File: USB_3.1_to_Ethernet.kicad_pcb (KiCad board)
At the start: 4 copper layers, 75 x 25 mm, 93 parts, among them J1 RJ45_JK0654219, J2 USB3_A, U1 LAN7801_9JX, U2 93LC56B_SN, U3 KSZ9031RNXCC, U4 TLV76733, U5 USBLC6-2P6, U6 TPS7A0212, Y1 25MHz, Y2 25MHz

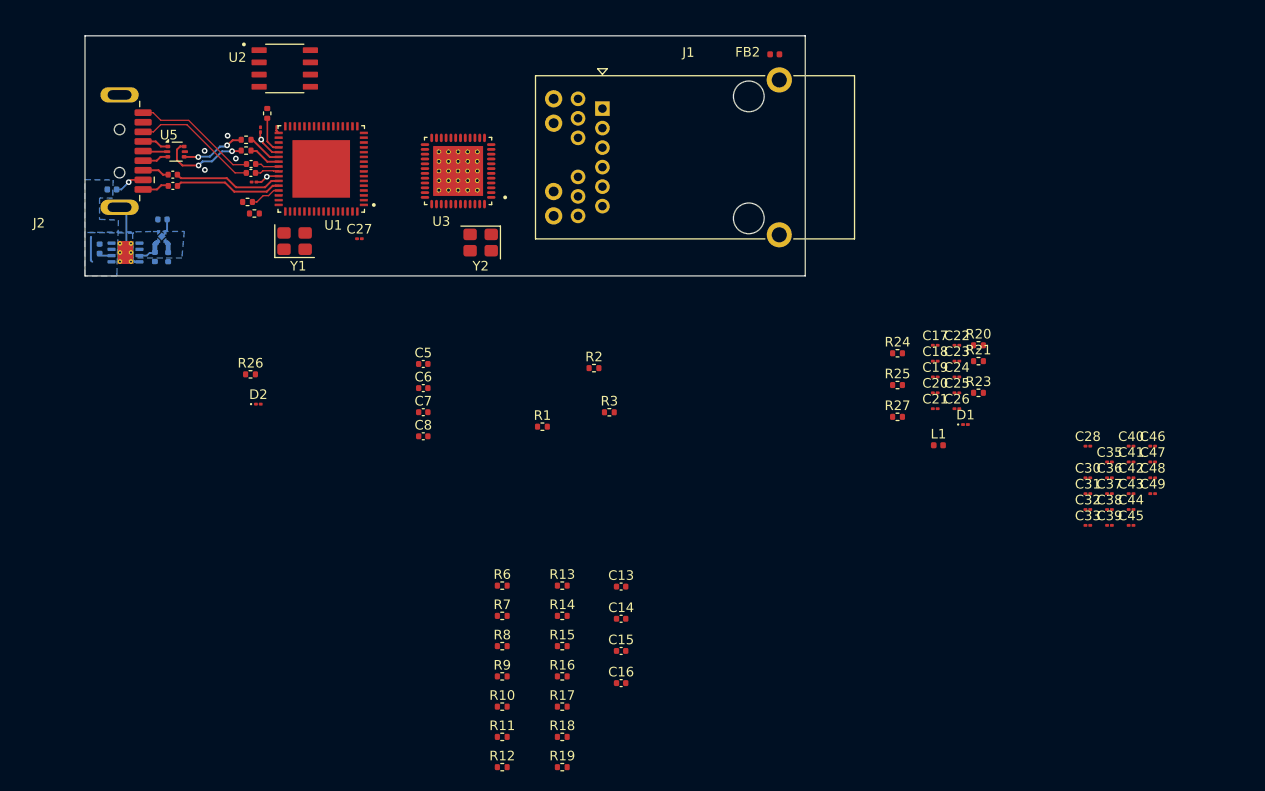
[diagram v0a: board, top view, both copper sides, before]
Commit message: 1. usb routing done 2.clock routing done 3. decoupling capacitors(3.3v) routing for lan7801 ic done
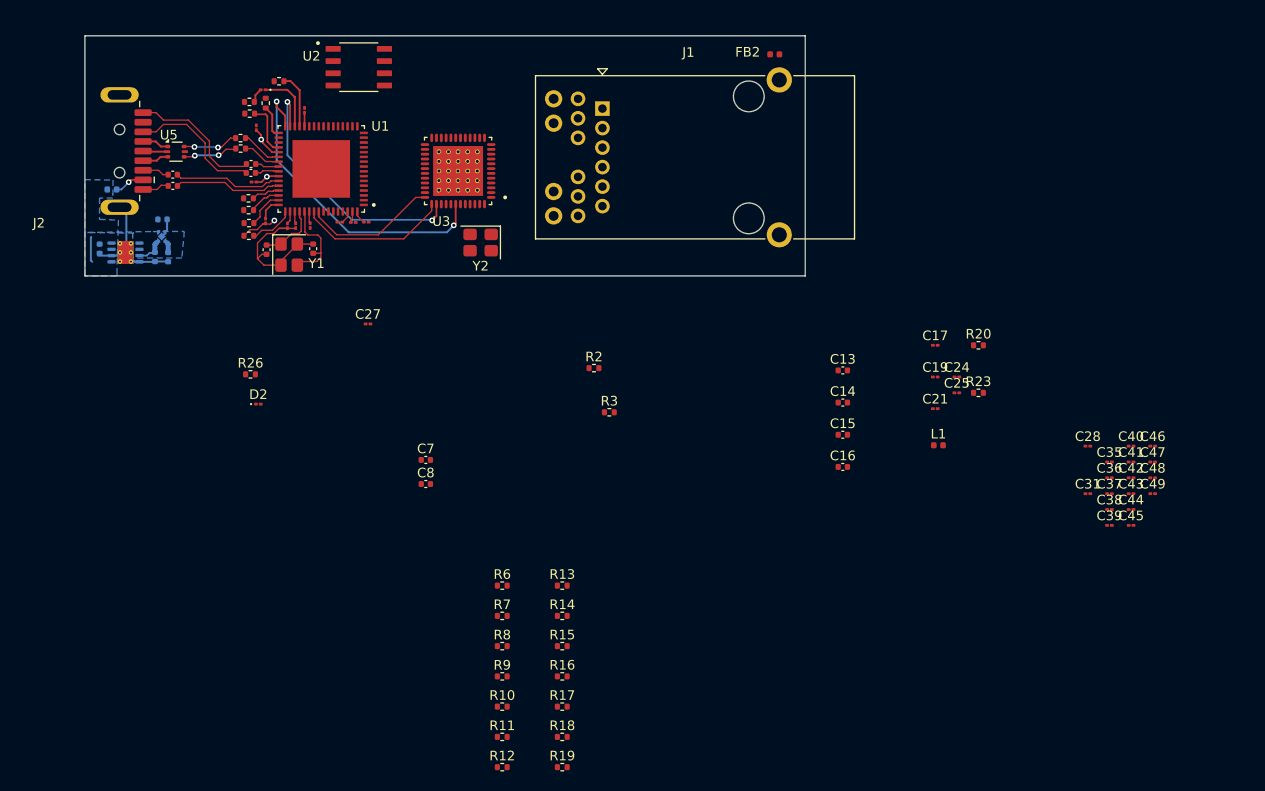
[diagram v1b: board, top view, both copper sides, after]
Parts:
- moved C30 90.1 mm to (82.6, 57.9), turned to 90 degrees
- moved C33 86.8 mm to (83.2, 69.9), turned to -90 degrees
- moved C32 83.4 mm to (86.2, 69.5), turned to 180 degrees
- moved D1 81.0 mm to (78.2, 55.7), turned to 180 degrees
- moved R21 78.9 mm to (78.5, 57.1), turned to -90 degrees
- moved R25 73.6 mm to (76.8, 57.0), turned to 180 degrees
- moved C18 71.2 mm to (78.5, 69.4), turned to -90 degrees
- moved C22 70.8 mm to (80.8, 69.9), turned to -90 degrees
- moved R27 70.5 mm to (76.8, 69.6), turned to 180 degrees
- moved R24 70.3 mm to (79.9, 54.8)
- moved C23 70.3 mm to (81.6, 69.9), turned to -90 degrees
- moved C26 65.8 mm to (87.6, 69.5)
- moved C20 61.9 mm to (89.0, 69.5)
- moved R1 36.5 mm to (76.8, 70.9), turned to 180 degrees
- moved C13 32.2 mm to (138.6, 84.9)
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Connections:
- C40 pad 1: Net-(C40-Pad1) -> 1v2_core
- C41 pad 1: Net-(C40-Pad1) -> 1v2_core
- C42 pad 1: Net-(C40-Pad1) -> 1v2_core
- C43 pad 1: Net-(C40-Pad1) -> 1v2_core
- C44 pad 1: Net-(C40-Pad1) -> 1v2_core
- C45 pad 1: Net-(C40-Pad1) -> 1v2_core
- C46 pad 1: Net-(C40-Pad1) -> 1v2_core
- C47 pad 1: Net-(C40-Pad1) -> 1v2_core
- C48 pad 1: Net-(C40-Pad1) -> 1v2_core
- C49 pad 1: Net-(C40-Pad1) -> 1v2_core
- R4 pad 2: D- -> D+
- R5 pad 2: D+ -> D-
- R6 pad 2: /TXD3 -> /TXD3_phy
- R7 pad 2: /TXD2 -> /TXD2_phy
- R8 pad 2: /TXD1 -> /TXD1_phy
- R9 pad 2: /TXD0 -> /TXD0_phy
- U3 pad 19: /TXD0 -> /TXD0_phy
- U3 pad 20: /TXD1 -> /TXD1_phy
- U3 pad 21: /TXD2 -> /TXD2_phy
- U3 pad 22: /TXD3 -> /TXD3_phy
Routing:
- net /~{RESET_N}: track 0.00 -> 33.2 mm, vias 0 -> 2
- net /INT_N/PME_N2: track 0.00 -> 28.0 mm, vias 0 -> 2
- net GND: track 12.8 -> 37.1 mm, vias 0 -> 1
- net /MDIO: track 0.00 -> 15.7 mm
- net /MDC: track 0.00 -> 14.0 mm
- net /XO_LAN: track 0.00 -> 9.68 mm
- net /~{SUSPEND_N}: track 0.00 -> 6.52 mm
- net 3v3_out: track 3.95 -> 10.3 mm
- net /XI_LAN: track 0.00 -> 6.31 mm
- net Net-(U1-VBUS_DET): track 0.00 -> 5.80 mm
- net Net-(U1-USBRBIAS): track 0.00 -> 4.69 mm
- net 1v2_core: track 5.81 -> 10.3 mm
- net Net-(U1-~{RESET_N}/PME_CLEAR): track 0.00 -> 3.96 mm
- net /Power section/_P: track 9.55 -> 5.81 mm
- net Net-(U1-TEST): track 0.00 -> 3.39 mm
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
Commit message: 1. RGMII routing done - LAN7801 RXD 2.Routing for RGMII - TXD on top layer done, bottom layer remaining 3. source termination resistors 27 ohm removed for RGMII
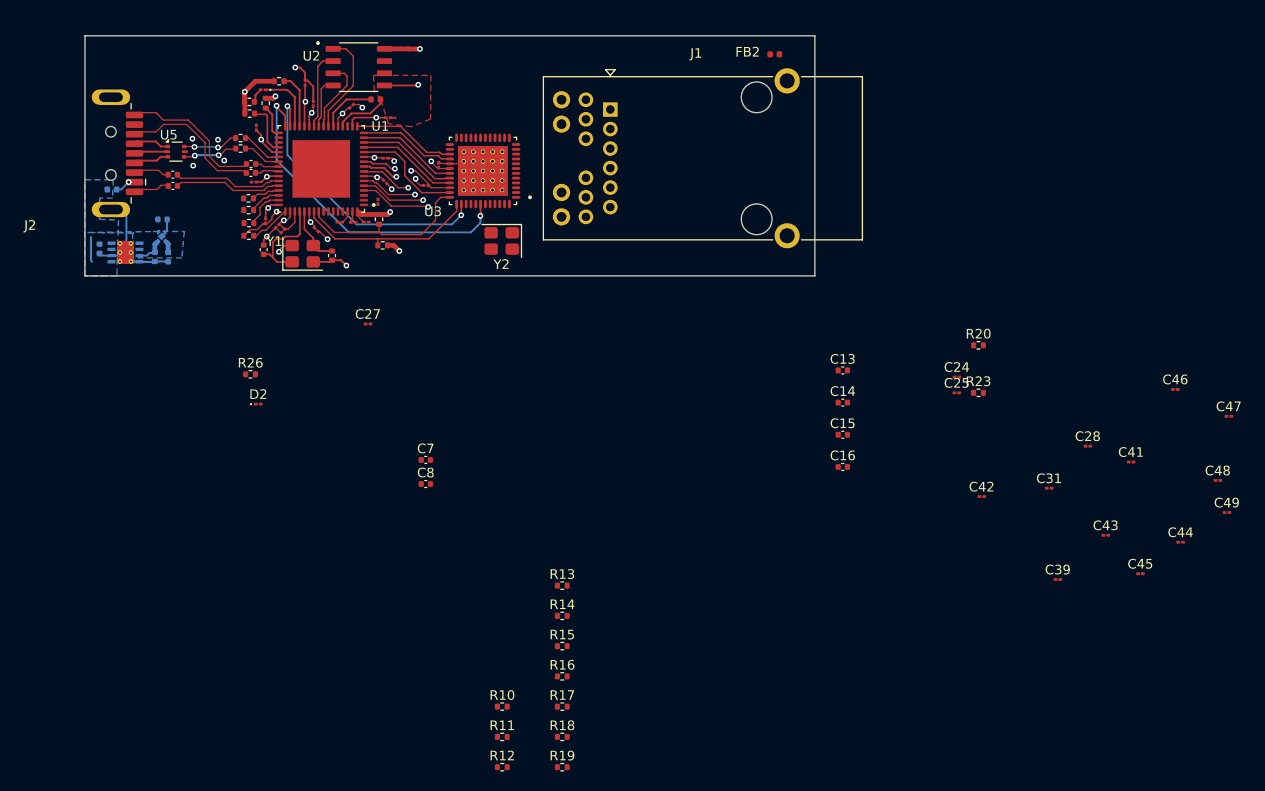
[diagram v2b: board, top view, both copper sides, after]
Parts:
- removed R6, R7, R8, R9: 27R, Resistor_SMD:R_0402_1005Metric
- moved C35 90.9 mm to (83.5, 57.2), turned to 90 degrees
- moved C38 85.5 mm to (91.3, 58.6)
- moved C36 81.4 mm to (90.2, 67.4), turned to -90 degrees
- moved C37 78.1 mm to (95.2, 65.7), turned to 180 degrees
- moved C40 77.8 mm to (96.5, 63.6), turned to 90 degrees
- moved L1 68.8 mm to (90.0, 56.7)
- moved C17 65.7 mm to (87.5, 57.4), turned to 45 degrees
- moved C21 62.0 mm to (91.0, 65.3), turned to -45 degrees
- moved C19 61.6 mm to (91.0, 62.9)
- moved R3 29.3 mm to (90.7, 71.9), turned to 180 degrees
- moved R2 27.2 mm to (90.3, 69.2), turned to -90 degrees
- moved C42 15.7 mm to (153.1, 98.1)
- moved C47 9.25 mm to (178.8, 89.7)
- moved C49 7.98 mm to (178.6, 99.7)
- moved C39 7.78 mm to (161.0, 106.7)
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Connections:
- U1 pad 9: /TX_CTL -> /GTX_CLK
- U3 pad 19: /TXD0_phy -> /TXD0
- U3 pad 20: /TXD1_phy -> /TXD1
- U3 pad 21: /TXD2_phy -> /TXD2
- U3 pad 22: /TXD3_phy -> /TXD3
- U3 pad 25: /TX_EN -> /TXC
- U3 pad 27: /RXD3/MODE3 -> /RXD3
- U3 pad 28: /RXD2/MODE2 -> /RXD2
- U3 pad 31: /RXD1/MODE1 -> /RXD1
- U3 pad 32: /RXD0/MODE0 -> /RXD0
- U3 pad 33: /RX_DV/CLK125_EN -> /RX_CTL
- U3 pad 35: /RX_CLK/PHYAD2 -> /RXC
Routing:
- net 3v3_out: track 10.3 -> 83.4 mm, vias 0 -> 13
- net GND: track 37.1 -> 72.9 mm, vias 1 -> 11
- net 1v2_core: track 10.3 -> 37.1 mm, vias 2 -> 5
- net /RXC: track 0.00 -> 11.6 mm
- net /RXD3: track 0.00 -> 10.8 mm
- net /CS: track 0.00 -> 10.8 mm
- net /RXD0: track 0.00 -> 10.5 mm
- net /RX_CTL: track 0.00 -> 10.5 mm
- net /RXD1: track 0.00 -> 10.5 mm
- net /RXD2: track 0.00 -> 10.1 mm
- net /CLK: track 0.00 -> 8.24 mm
- net /DI: track 0.00 -> 7.81 mm
- net /TXD3: track 0.00 -> 7.41 mm, vias 0 -> 1
- net /TXD2: track 0.00 -> 6.80 mm, vias 0 -> 1
- net Net-(U1-VDD12_SW_FB): track 0.00 -> 5.93 mm
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- added copper zone on F.Cu, net GND
- added copper zone on In1.Cu, net GND
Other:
- board size 75 x 25 mm -> 76 x 25 mm

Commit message: rgmii routing completed
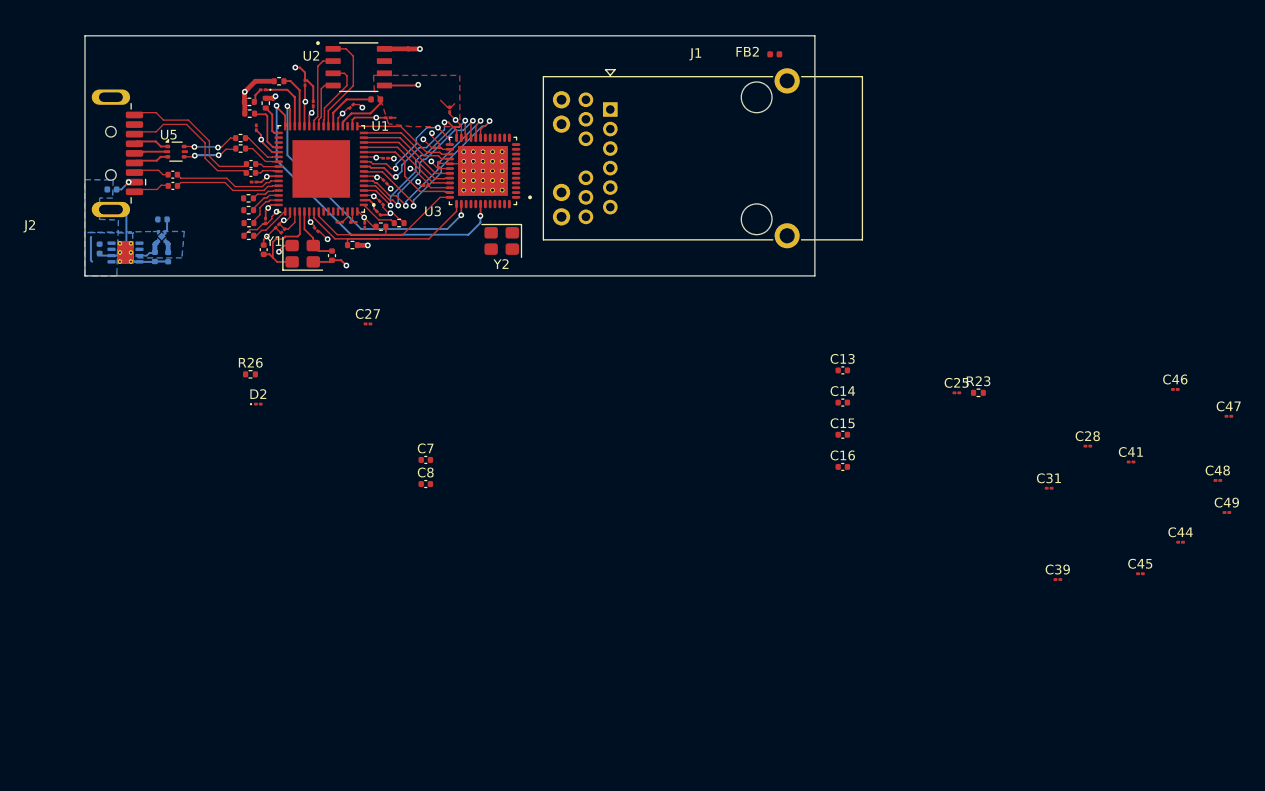
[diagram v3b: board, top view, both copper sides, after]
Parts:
- removed R10, R11, R12, R13, R14, R15, R16, R17, R18, R19: 27R, Resistor_SMD:R_0402_1005Metric
- moved C43 80.5 mm to (96.3, 61.8), turned to 180 degrees
- moved C42 68.5 mm to (97.7, 57.8), turned to 90 degrees
- moved C24 62.6 mm to (90.3, 68.6), turned to -45 degrees
- moved R20 61.7 mm to (92.4, 69.6)
- moved R3 3.15 mm to (87.5, 71.9)
- moved R2 0.79 mm to (90.5, 70.0), turned to 0 degrees
- moved C36 0.37 mm to (90.6, 67.5), turned to -45 degrees
- moved C20 0.36 mm to (88.8, 69.8), turned to -90 degrees
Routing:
- net /TXD0: track 5.33 -> 21.4 mm, vias 1 -> 2
- net /TXD1: track 5.92 -> 19.5 mm, vias 1 -> 2
- net /TXD2: track 6.80 -> 19.1 mm, vias 1 -> 2
- net /TXD3: track 7.41 -> 17.9 mm, vias 1 -> 2
- net /GTX_CLK: track 3.88 -> 14.4 mm, vias 1 -> 2
- net /TXC: track 3.72 -> 12.6 mm, vias 1 -> 2
- net GND: track 72.9 -> 80.0 mm, vias 11 -> 13
- net 1v2_core: track 37.1 -> 43.2 mm, vias 5 -> 7
- net Net-(U1-REF_REXT): track 0.00 -> 3.95 mm
- net /MDIO: track 19.0 -> 22.1 mm
- net Net-(U1-REF_FILT): track 0.00 -> 2.09 mm
- net /MDC: track 18.5 -> 17.4 mm
- net 3v3_out: vias 13 -> 14
- net (no net): vias 4 -> 0

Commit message: 1.complete routing done 2.Ethernet  MDI differential routing done 3.power and gnd  plane on L2 and L3 completed 4.
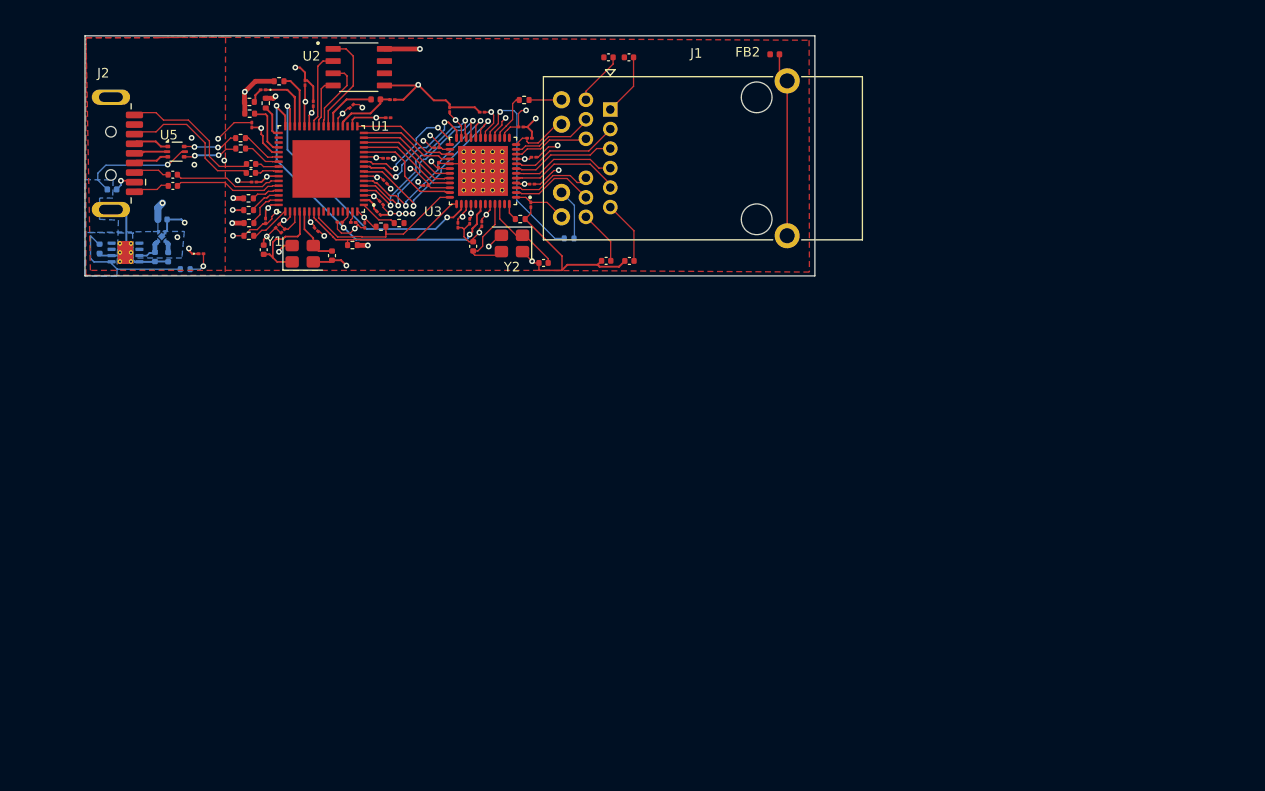
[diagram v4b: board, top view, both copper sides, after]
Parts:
- removed C28: 4.7uF, Capacitor_SMD:C_01005_0402Metric
- removed C44: 0.1uF, Capacitor_SMD:C_01005_0402Metric
- added R18: 27R, Resistor_SMD:R_0402_1005Metric, B.Cu at (110.1, 71.2)
- added R19: 27R, Resistor_SMD:R_0402_1005Metric, F.Cu at (105.4, 56.8)
- R26: moved to B.Cu
- moved C49 82.4 mm to (106.0, 60.8)
- moved C48 81.4 mm to (105.1, 59.6)
- moved C45 77.7 mm to (101.0, 69.7), turned to -90 degrees
- moved C47 77.2 mm to (106.4, 62.7)
- moved C41 74.3 mm to (98.5, 69.8), turned to -90 degrees
- moved C39 71.7 mm to (99.8, 69.4), turned to -90 degrees
- moved C31 70.9 mm to (101.0, 58.0), turned to 180 degrees
- moved C46 70.3 mm to (106.2, 65.5)
- moved C25 66.2 mm to (91.7, 56.8)
- moved R23 51.0 mm to (105.0, 69.2)
- moved C16 49.1 mm to (114.2, 52.3)
- moved C15 45.2 mm to (116.3, 52.3)
- moved C13 27.2 mm to (114.0, 73.5)
- moved C14 26.7 mm to (116.4, 73.5)
- moved C8 25.2 mm to (100.1, 72.0), turned to -90 degrees
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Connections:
- net /TXRXM_A renamed /A_-
- net /TXRXM_C renamed /C_-
- net /TXRXP_A renamed /A_+
- net /TXRXP_C renamed /C_+
- C48 pad 1: 1v2_core -> 3v3_out
- C49 pad 1: 1v2_core -> 3v3_out
- J1 pad 4: /TXRXP_B -> /B_+
- J1 pad 5: /TXRXM_B -> /B_-
- J1 pad 8: /TXRXP_D -> /D_-
- J1 pad 9: /TXRXM_D -> /D_+
- U3 pad 10: /TXRXP_D -> /D_+
- U3 pad 11: /TXRXM_D -> /D_-
- U3 pad 5: /TXRXP_B -> /B_-
- U3 pad 6: /TXRXM_B -> /B_+
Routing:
- net 1v2_core: track 43.2 -> 125.4 mm, vias 7 -> 15
- net GND: track 80.0 -> 144.6 mm, vias 13 -> 32
- net 3v3_out: track 83.4 -> 126.2 mm, vias 14 -> 19
- net +5V: track 0.00 -> 25.6 mm, vias 0 -> 1
- net /LED1/PHYAD0/PME_N1: track 0.00 -> 20.9 mm, vias 0 -> 1
- net GNDPWR: track 0.00 -> 19.2 mm
- net /B_-: track 0.00 -> 11.6 mm
- net /C_-: track 0.00 -> 11.5 mm
- net /B_+: track 0.00 -> 10.8 mm
- net /C_+: track 0.00 -> 10.8 mm
- net /XO_PHY: track 0.00 -> 9.55 mm
- net /A_+: track 0.00 -> 8.79 mm
- net /XI_PHY: track 0.00 -> 8.74 mm
- net /D_-: track 0.00 -> 8.69 mm
- net /A_-: track 0.00 -> 8.46 mm
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- added copper zone on In2.Cu, net 1v2_core
- added copper zone on In2.Cu, net 3v3_out
